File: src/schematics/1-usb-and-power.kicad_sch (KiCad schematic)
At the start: 62 parts, among them Q2 NX6008NBKW, U2 MP5016HGQH, U3 BQ24392RSER, U4 FUSB302BMPX, U6 TPS628512DRLR

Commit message: Further elaboration of the USB / power module schematics.
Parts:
- removed C54, C55, C58, C59: 22μF, restall-generic-capacitors:unpolarised-nominal-0402-1005, symbol restall-generic-capacitors:capacitor-unpolarised
- removed C56, C57, C60, C61: 4.7μF, restall-generic-capacitors:unpolarised-nominal-0402-1005, symbol restall-generic-capacitors:capacitor-unpolarised
- removed C_PLANE1, C_PLANE2: ${SIM.PARAMS}, restall-generic-capacitors:unpolarised-nominal-0402-1005, symbol restall-generic-capacitors:capacitor-unpolarised
- removed FB2: WLBD2012HCU601TH, restall-manufacturer-walsin:WLBD2012, symbol restall-manufacturer-walsin:WLBD2012HCU121TH
- removed FB3: WLBD2012HCU121TH, restall-manufacturer-walsin:WLBD2012, symbol restall-manufacturer-walsin:WLBD2012HCU121TH
- removed L_VIA10, L_VIA11, L_VIA12, L_VIA13, L_VIA14, L_VIA15, L_VIA8, L_VIA9: ${SIM.PARAMS}, symbol restall-generic-inductors:l-air
- added C123, C124: 4.7μF, restall-generic-capacitors:unpolarised-nominal-0402-1005, symbol restall-generic-capacitors:capacitor-unpolarised
- added C125, C126: 22μF, restall-generic-capacitors:unpolarised-nominal-0805-2012, symbol restall-generic-capacitors:capacitor-unpolarised
- added C127: 10pF, restall-generic-capacitors:unpolarised-nominal-0402-1005, symbol restall-generic-capacitors:capacitor-unpolarised
- added R112: 88.7kΩ, restall-generic-resistors:nominal-0402-1005, symbol restall-generic-resistors:resistor
- added R113: 19.6kΩ, restall-generic-resistors:nominal-0402-1005, symbol restall-generic-resistors:resistor
- renumbered C27 to C101, C28 to C102, C35 to C103, C23 to C104, C24 to C105, C41 to C106, C25 to C107, C26 to C108, C30 to C109, C31 to C110, C36 to C111, C37 to C112, C38 to C113, C34 to C114, C33 to C115, C29 to C116, C40 to C117, C63 to C118, C62 to C119, C43 to C120, C44 to C121, C42 to C122, D8 to D101, Q2 to Q101, R21 to R101, R22 to R102, R23 to R103, R26 to R104, R27 to R105, R28 to R106, R24 to R107, R25 to R108, R33 to R109, R30 to R110, R32 to R111, R31 to R114, U2 to U101, U3 to U102, U4 to U103, U6 to U104
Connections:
- net CORE_VDD_{+3.3V}: now also L101.2 (P2), R114.1, C123.1, C124.1, C125.1, C126.1, C127.1, R112.1
- net CORE_VDD_{+5V}: now also FB101.1 (P1); no longer C116.1, C117.1, C118.1, C119.1, C120.1, D101.1 (K), R110.1, U104.1 (V_{IN})
- net GND: now also C123.2, C124.2, C125.2, C126.2, R113.2
- net at FB101.2 (P2): now also C116.1, C117.1, C118.1, C119.1, C120.1, D101.1 (K), R110.1, U104.1 (V_{IN})
- net at U104.5 (FB): now also C127.2, R112.2, R113.1
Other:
- note added: "Budget: 3.12V_{dc}-3.52V_{dc} 600mA_{dc}"
- note added: "Budget: 4.15V_{dc}-6V_{dc} 830mA_{dc}"
- note added: "Core voltage regulator for +3.3V logic (DC:DC synchronous buck converter)"
- note added: "Primary means of supply input protection (OVP and OCP) as well as USB inrush current limiting and soft-start mechanism"
- note added: "TODO: VERIFY C_{eff} ON CORE_VDD_{+5V} IS <90uF"
- note added: "TODO: VERIFY LABEL CORE_VDD_{+3.3V} AND HIERARCHY PIN OF SAME NAME ARE ACTUALLY THE SAME NET !"
- note added: "USB Type-C, PD, BC and data interfaces"
- note added: "USB VBUS: 4.23V_{dc}-20V_{dc} Default Load: 100mA_{dc} Enumerated Load: 500mA_{dc} Charger Load: 1.5A_{dc}"
- note added: "Unless otherwise specified: All resistors and capacitors are 0402 All resistors are ±1% 100ppm 0.625W thick-film All capacitors are ±20% X5R 10V MLCC"
- note added: "Webench simulation suggests around 0.25W dissipation in TPS628512 at full 1.5A load"
- note removed: "TODO: MOVE FB101 INTO CORE_VDD_{+5V} - BUT LEAVE C30 / C29 NEXT TO MP5016H ? SIMULATE..."
- note removed: "TODO: POWER SUPPLIES. TPS62441 is a dual buck converter - two independent outputs with high switching frequency (ie. low value / small inductors). One output should be an always-enabled +3.3V -> LC pi filter -> digital One output should be an MCU-enabled +3.954V_{absmin} -> LC pi filter -> TPS7A20 -> +3.6V -> analogue (radio and vrefs) For pi filters, use L with SRF >> 2.5MHz (preferably > 100MHz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"
- note removed: "TODO: SIMULATE CURRENT PULSES OF 4A FOR 50ns @ 2.25MHz ON THE INPUT BYPASS (FOR RIPPLE) AND ON THE STEADY-STATE CURRENT DRAWN FROM THE USB RAIL. IF THE CURRENT DRAWN FROM THE USB RAIL > THE MP5016H CURRENT LIMIT THEN IT WILL TRIP...NOT GOOD."
- note removed: "TODO: TO BUCK OUTPUT..."
- note removed: "TODO: WEBENCH SUGGESTS 0.25W DISSIPATION FOR TPS628512 !"
- moved on the sheet: C101, C102, C103, C104, C105, C106, C107, C108, C109, C110, C111, C112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

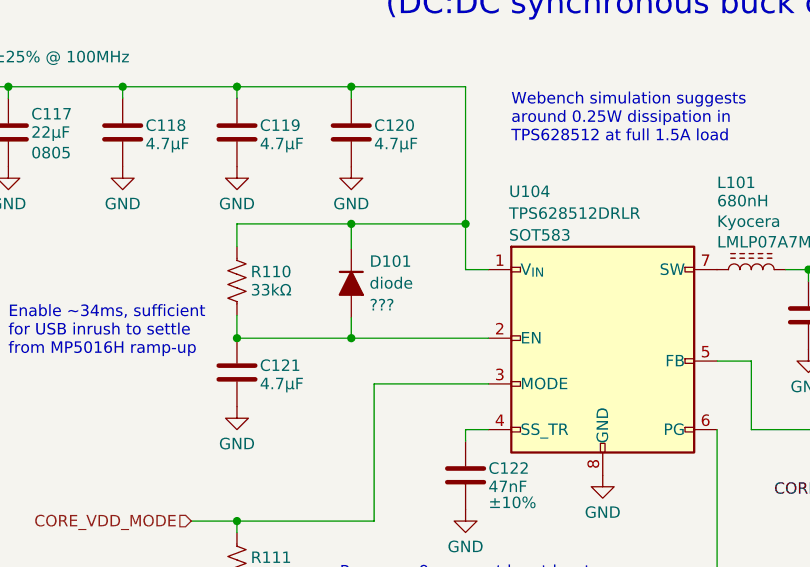
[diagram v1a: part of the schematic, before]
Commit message: Started to draw the MSF receiver based on the simulation learnings.
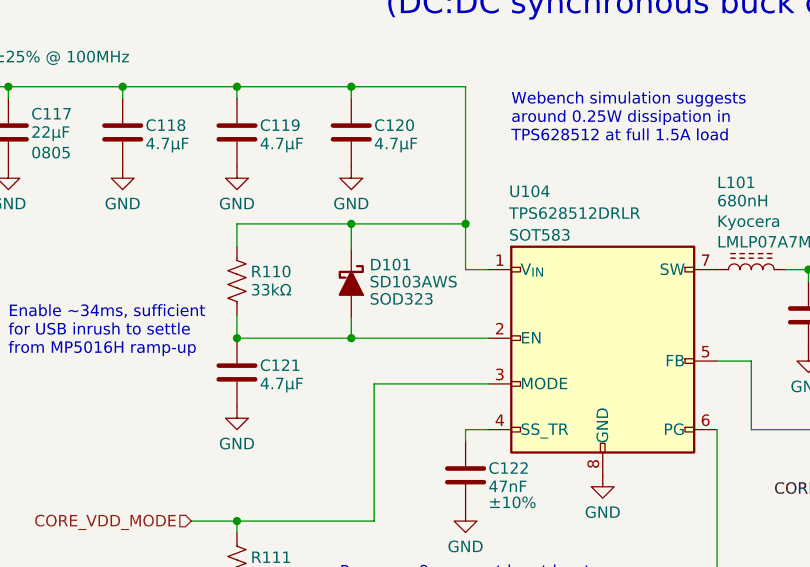
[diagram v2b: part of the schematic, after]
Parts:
- removed D101: diode, symbol restall-generic-diodes:diode
- added D101: SD103AWS, restall-generic-sot:SOD-323, symbol restall-generic-diodes:schottky
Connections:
- net at C116.1, C117.1, C118.1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: now also D101.1 (K)
- net at C121.1, R110.2, U104.2 (EN): now also D101.2 (A)
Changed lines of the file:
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@@
-    )
-  )
-  (symbol (lib_id "restall-generic-diodes:diode") (at 91.44 214.884 270) (unit 1)
-    (in_bom yes) (on_board yes) (dnp no) (fields_autoplaced)
-    (property "Reference" "D101" (at 93.472 212.4598 90)
-      (effects (font (size 1.27 1.27)) (justify left))
-    )
-    (property "Value" "diode" (at 93.472 214.884 90)
-      (effects (font (size 1.27 1.27)) (justify left))
-    )
-    (property "Footprint" "" (at 91.44 214.884 0)
-      (effects (font (size 1.27 1.27)) hide)
-    )
-    (property "Datasheet" "~" (at 91.44 214.884 0)
-      (effects (font (size 1.27 1.27)) hide)
-    )
-    (property "Package" "???" (at 93.472 217.3082 90)
-      (effects (font (size 1.27 1.27)) (justify left))
-    )
-    (property "Manufacturer" "" (at 91.44 214.884 0)
-      (effects (font (size 1.27 1.27)) (justify left) hide)
-    )
-    (property "ManufacturerPartNumber" "" (at 91.44 214.884 0)
-      (effects (font (size 1.27 1.27)) (justify left) hide)
-    )
-    (property "Manufacturer2" "" (at 91.44 214.884 0)
-      (effects (font (size 1.27 1.27)) (justify left) hide)
-    )
-    (property "Manufacturer2PartNumber" "" (at 91.44 214.884 0)
-      (effects (font (size 1.27 1.27)) (justify left) hide)
-    )
-    (pin "2")
-    (pin "1")
-    (instances
-      (project "msf-owl-clock"
-        (path "/56d623d3-22db-4d43-a9d9-e6bb4bb68946/93bae52d-c1e4-402b-b299-c5014664f19e"
-          (reference "D101") (unit 1)
-        )
-      )
     )
   )
@@
         )
       )
+    )
+  )
+  (symbol (lib_id "restall-generic-diodes:schottky") (at 91.44 214.884 270) (unit 1)
+    (in_bom yes) (on_board yes) (dnp no)
+    (property "Reference" "D101" (at 93.472 212.852 90)
+      (effects (font (size 1.27 1.27)) (justify left))
+    )
+    (property "Value" "SD103AWS" (at 93.472 214.7458 90)
+      (effects (font (size 1.27 1.27)) (justify left))
+    )
+    (property "Footprint" "restall-generic-sot:SOD-323" (at 91.44 214.884 0)
+      (effects (font (size 1.27 1.27)) (justify right) hide)
+    )
+    (property "Datasheet" "https://mm.digikey.com/Volume0/opasdata/d220001/medias/docus/5534/SD103AWS%20thru%20SD103CWS.pdf" (at 91.44 214.884 0)
+      (effects (font (size 1.27 1.27)) (justify right) hide)
+    )
+    (property "Package" "SOD323" (at 93.472 216.662 90)
+      (effects (font (size 1.27 1.27)) (justify left))
+    )
+    (property "Manufacturer" "Evvo Semi" (at 91.44 214.884 0)
+      (effects (font (size 1.27 1.27)) (justify right) hide)
+    )
+    (property "ManufacturerPartNumber" "SD103AWS" (at 91.44 214.884 0)
+      (effects (font (size 1.27 1.27)) (justify right) hide)
+    )
+    (property "Manufacturer2" "Anbon Semiconductor" (at 91.44 214.884 0)
+      (effects (font (size 1.27 1.27)) (justify right) hide)
+    )
+    (property "Manufacturer2PartNumber" "SD103AWS" (at 91.44 214.884 0)
+      (effects (font (size 1.27 1.27)) (justify right) hide)
+    )
+    (pin "2")
+    (pin "1")
+    (instances
+      (project "msf-owl-clock"
+        (path "/56d623d3-22db-4d43-a9d9-e6bb4bb68946/93bae52d-c1e4-402b-b299-c5014664f19e"
+          (reference "D101") (unit 1)
+        )
+      )
